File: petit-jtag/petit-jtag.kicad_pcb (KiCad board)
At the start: 2 copper layers, 28.6 x 33.7 mm, 9 parts, among them CON101 JTAG-2X3-1.27MM-HDR, CON102 USB-B1HSB6, CON103 JTAG-2X5-HDR-SHROUD, CON104 HDR1X3, U101 AZ1117CH-3.3TRG1

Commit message: mostly done v1.0
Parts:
- logo101: footprint db-artwork:db-logo_10mm -> db-artwork:db-logo_7.5mm
- moved logo101 2.77 mm to (150.0, 113.3)
- moved C102 0.52 mm to (158.2, 97.2)
- moved logo102 0.36 mm to (169.5, 114.2)
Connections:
- CON103 pad 4: VCC -> +3V3
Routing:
- net /TDO: track 0.00 -> 39.7 mm
- net +3V3: track 0.00 -> 30.3 mm, vias 0 -> 1
- net /TCK: track 0.00 -> 29.0 mm
- net VCC: track 0.00 -> 27.5 mm
- net /TMS: track 0.00 -> 26.7 mm
- net /TDI: track 0.00 -> 18.7 mm
- net +5V: track 0.00 -> 15.0 mm
- net GND: track 0.00 -> 0.04 mm, vias 0 -> 3
- added copper zone on B.Cu, net GND
- added copper zone on F.Cu, net GND
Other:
- board text added: "GND VCC TMS"
- board text added: "TDO TCK TDI"
- board text added: "VCC"
- board text added: "db electronics petit jtag v1.0 2023-12.28"
- board text removed: "db electronics"
- board text removed: "petit jtag v1.0 2023.12.28"

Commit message: version 1.0 ready
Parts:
- added CON105: HDR1X2, db-thparts:HDR1X2, F.Cu at (153.4, 88.4)
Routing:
- net +5V: track 15.0 -> 21.0 mm
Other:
- board text added: "+"
- board text added: "-"
- board text added: "db electronics petit jtag v1.0 2023.12.28"
- board text removed: "db electronics petit jtag v1.0 2023-12.28"
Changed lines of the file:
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@@
   )
   (paper "A4")
+  (title_block
+    (title "Petit JTAG")
+    (date "2023-12-28")
+    (rev "1.0")
+    (company "db electronics")
+    (comment 1 "https://github.com/db-electronics/petit-jtag-kicad")
+    (comment 2 "Licensed under CERN OHL v.1.2")
+    (comment 3 "Copyright René Richard 2023")
+  )
   (layers
     (0 "F.Cu" signal)
@@
     (aux_axis_origin 145.415 119.38)
     (pcbplotparams
-      (layerselection 0x00010fc_ffffffff)
+      (layerselection 0x00010f0_ffffffff)
       (plot_on_all_layers_selection 0x0000000_00000000)
       (disableapertmacros false)
-      (usegerberextensions false)
+      (usegerberextensions true)
       (usegerberattributes true)
       (usegerberadvancedattributes true)
@@
       (viasonmask false)
       (mode 1)
-      (useauxorigin false)
+      (useauxorigin true)
       (hpglpennumber 1)
       (hpglpenspeed 20)
@@
       (outputformat 1)
       (mirror false)
-      (drillshape 1)
+      (drillshape 0)
       (scaleselection 1)
-      (outputdirectory "")
+      (outputdirectory "gerbers/1.0")
     )
   )
@@
     (solder_mask_margin 0.1016)
     (attr through_hole)
-    (fp_text reference "CON103" (at 2.54 16.383) (layer "F.SilkS")
+    (fp_text reference "CON103" (at -4.191 12.7 90) (layer "F.SilkS")
         (effects (font (size 0.889 0.889) (thickness 0.2032)))
     )
@@
       (net 2 "GND") (pinfunction "GND") (pintype "power_in"))
   )
+  (footprint "db-thparts:HDR1X2" (layer "F.Cu")
+    (at 153.416 88.392 90)
+    (property "Description" "SIL VERTICAL PC TAIL PIN HEADER")
+    (property "Digikey" "952-2262-ND")
+    (property "Sheetfile" "petit-jtag.kicad_sch")
+    (property "Sheetname" "")
+    (property "ki_description" "2 pin header")
+    (solder_mask_margin 0.1016)
+    (attr through_hole)
+    (fp_text reference "CON105" (at 2.032 1.27 180) (layer "F.SilkS") hide
+        (effects (font (size 0.889 0.889) (thickness 0.2032)))
+    )
+    (fp_text value "HDR1X2" (at 1.27 -3.302 90) (layer "F.Fab") hide
+        (effects (font (size 0.889 0.889) (thickness 0.2032)))
+    )
+    (pad "1" thru_hole circle (at 0 0 90) (size 1.524 1.524) (drill 1.016) (layers "*.Cu" "*.Mask")
+      (net 1 "+5V") (pinfunction "1") (pintype "passive") (solder_mask_margin 0.1016))
+    (pad "2" thru_hole circle (at 0 2.54 90) (size 1.524 1.524) (drill 1.016) (layers "*.Cu" "*.Mask")
+      (net 2 "GND") (pinfunction "2") (pintype "passive") (solder_mask_margin 0.1016))
+  )
   (gr_line (start 173.99 85.725) (end 173.99 119.38)
     (stroke (width 0.1778) (type default)) (layer "Edge.Cuts"))
@@
   (gr_line (start 145.415 85.725) (end 173.99 85.725)
     (stroke (width 0.1778) (type default)) (layer "Edge.Cuts"))
+  (gr_text "-" (at 155.321 87.249) (layer "F.SilkS")
+    (effects (font (size 0.889 0.889) (thickness 0.1778) bold) (justify left bottom))
+  )
+  (gr_text "+" (at 152.781 87.249) (layer "F.SilkS")
+    (effects (font (size 0.889 0.889) (thickness 0.1778) bold) (justify left bottom))
+  )
   (gr_text "GND\nVCC\nTMS" (at 161.3154 117.2972) (layer "F.SilkS")
     (effects (font (size 0.889 0.889) (thickness 0.1778) bold) (justify left bottom))
   )
-  (gr_text "db electronics\npetit jtag v1.0\n2023-12.28" (at 146.05 118.2624) (layer "F.SilkS")
+  (gr_text "db electronics\npetit jtag v1.0\n2023.12.28" (at 146.05 118.2624) (layer "F.SilkS")
     (effects (font (size 0.7112 0.7112) (thickness 0.1524) bold) (justify left bottom))
   )
@@
     (style (thickness 0.15) (arrow_length 1.27) (text_position_mode 0) (extension_height 0.58642) (extension_offset 0.5) keep_text_aligned)
   )
+  (segment (start 153.436 93.11) (end 151.892 91.566) (width 0.3048) (layer "F.Cu") (net 1))
+  (segment (start 151.892 91.566) (end 151.892 89.916) (width 0.3048) (layer "F.Cu") (net 1))
   (segment (start 151.4475 97.028) (end 155.321 97.028) (width 0.3048) (layer "F.Cu") (net 1))
+  (segment (start 151.892 89.916) (end 153.416 88.392) (width 0.3048) (layer "F.Cu") (net 1))
   (segment (start 153.436 93.11) (end 151.4475 95.0985) (width 0.3048) (layer "F.Cu") (net 1))
   (segment (start 155.321 97.028) (end 155.815 97.522) (width 0.3048) (layer "F.Cu") (net 1))

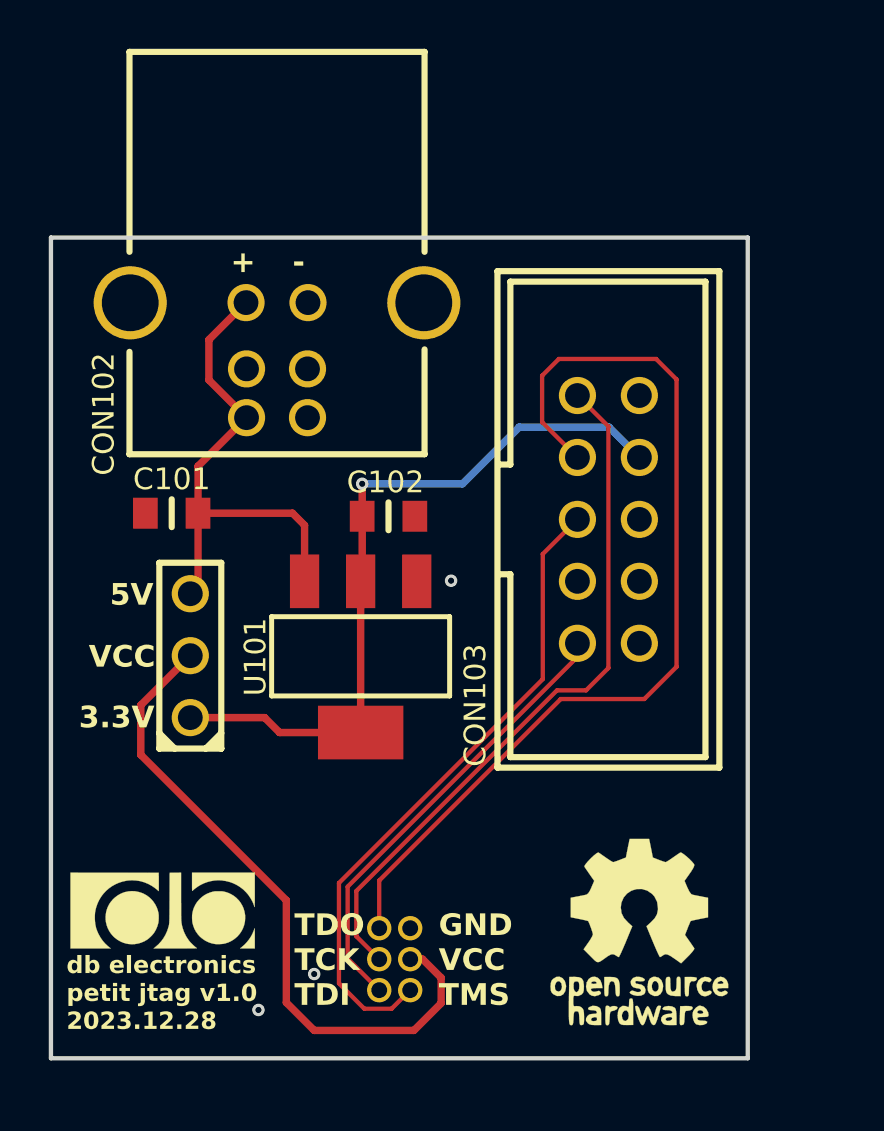
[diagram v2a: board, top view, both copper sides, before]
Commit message: updated with new staggered pin headers instead of 2x3
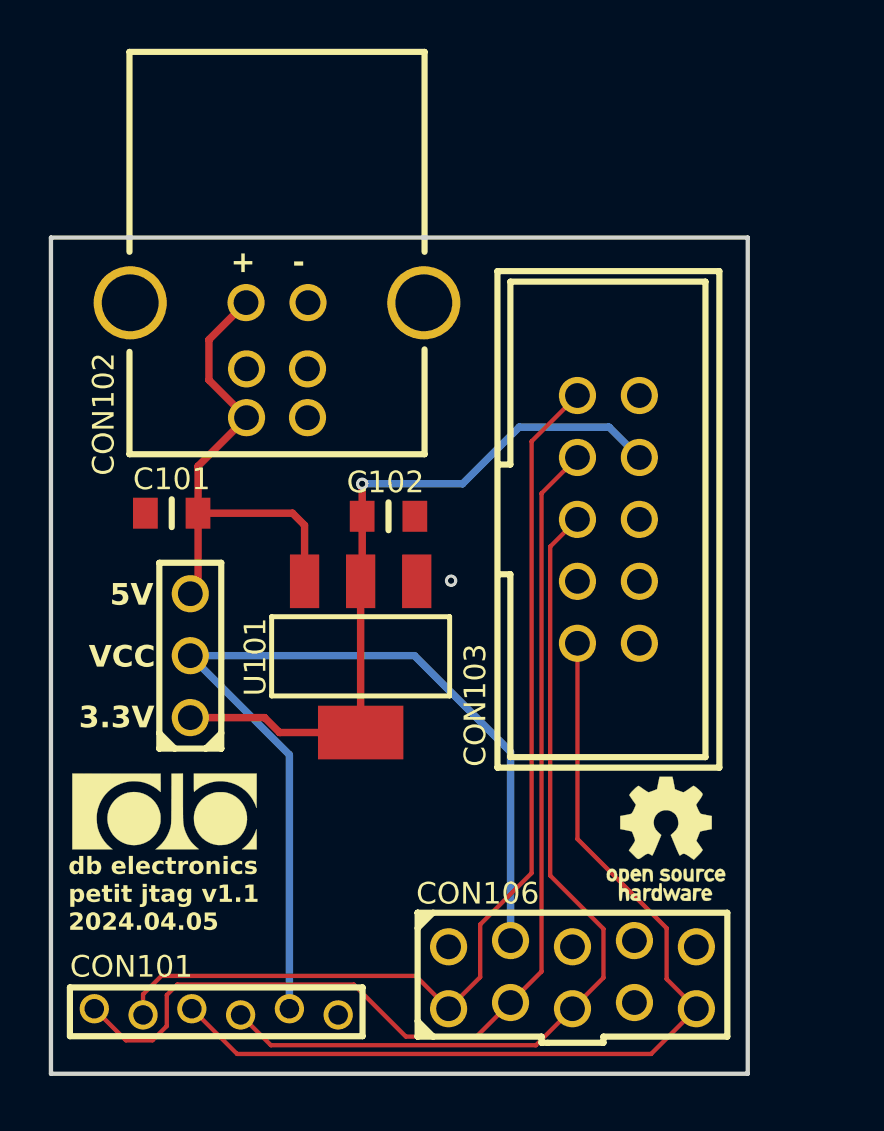
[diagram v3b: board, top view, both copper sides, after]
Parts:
- added CON106: HDR2X5, db-thparts:HDR2X5-JTAG, F.Cu at (161.7, 117.2)
- CON101: value JTAG-2X3-1.27MM-HDR -> JTAG-1X6-2MM-HDR; footprint db-thparts:HDR2X3_1.27MM -> db-thparts:HDR1X6_2MM
- logo102: footprint db-artwork:oshw-logo_7.5mm -> db-artwork:oshw-logo_5mm
- moved CON101 12.2 mm to (147.2, 117.5), turned to 90 degrees
- moved logo101 4.06 mm to (150.1, 109.3)
- moved logo102 3.96 mm to (170.6, 110.4)
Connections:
- CON101 pad 2: GND -> /TCK
- CON101 pad 3: /TCK -> /TDI
- CON101 pad 4: VCC -> /TMS
- CON101 pad 5: /TDI -> VCC
- CON101 pad 6: /TMS -> GND
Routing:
- net /TDI: track 18.7 -> 39.2 mm
- net /TCK: track 29.0 -> 41.6 mm
- net VCC: track 27.5 -> 38.7 mm
- net /TMS: track 26.7 -> 36.7 mm
- net /TDO: track 39.7 -> 44.2 mm
- net GND: vias 3 -> 1
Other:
- board size 28.6 x 33.7 mm -> 28.6 x 34.3 mm
- board text added: "db electronics petit jtag v1.1 2024.04.05"
- board text removed: "GND VCC TMS"
- board text removed: "TDO TCK TDI"
- board text removed: "db electronics petit jtag v1.0 2023.12.28"

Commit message: swd v1.0 sch complete, jtag v1.1 files
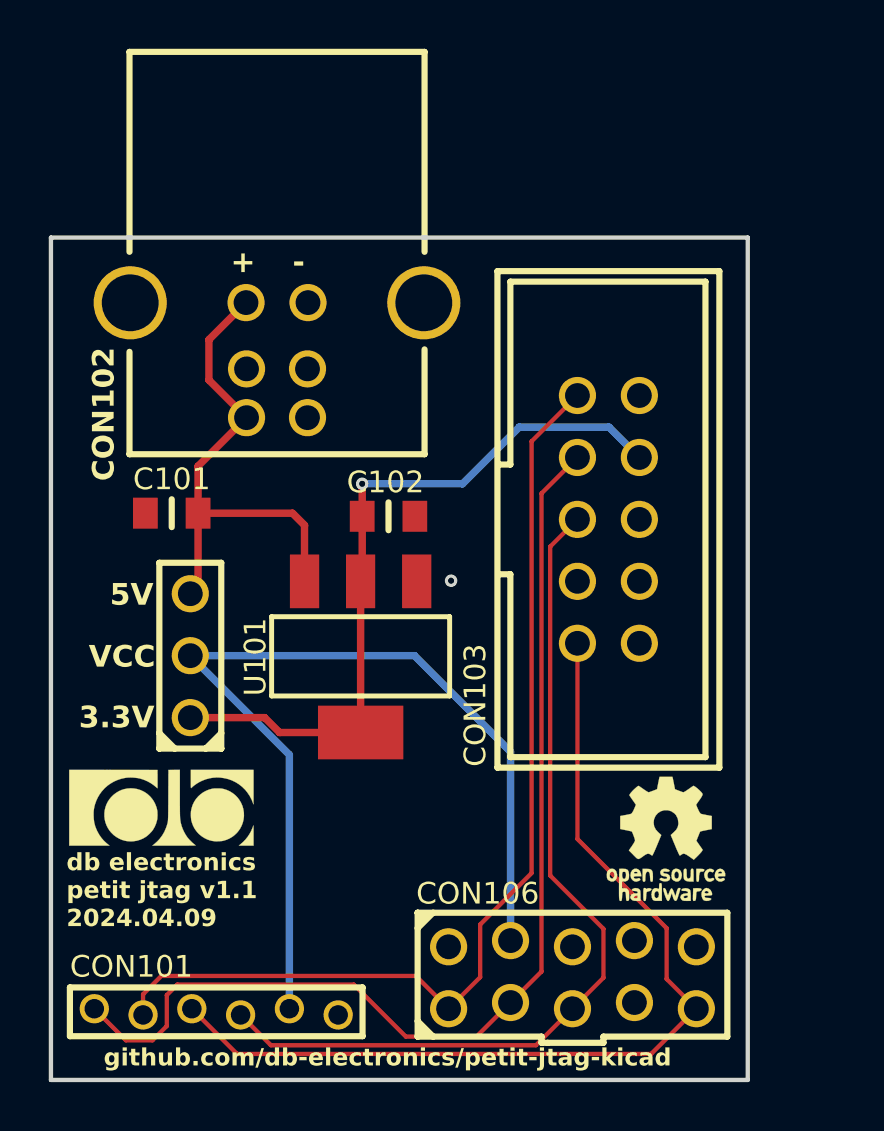
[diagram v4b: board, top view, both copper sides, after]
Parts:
- CON101: value JTAG-1X6-2MM-HDR -> 2PH1-06-UA
- CON103: value JTAG-2X5-HDR-SHROUD -> 302-S101
- CON104: value HDR1X3 -> 61300311121
- CON105: value HDR1X2 -> 61300211121
- CON106: value HDR2X5 -> 61301021121
- moved logo101 0.20 mm to (150.0, 109.1)
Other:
- board size 28.6 x 34.3 mm -> 28.6 x 34.5 mm
- board text added: "db electronics petit jtag v1.1 2024.04.09"
- board text added: "github.com/db-electronics/petit-jtag-kicad"
- board text removed: "db electronics petit jtag v1.1 2024.04.05"
